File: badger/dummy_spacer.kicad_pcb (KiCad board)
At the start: 2 copper layers, 200 x 200 mm, 12 parts

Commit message: badger upgrades
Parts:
- removed H12: MountingHole, MountingHole:MountingHole_6mm
- moved H11 31.7 mm to (-93.0, 0.00)
- moved H1 2.83 mm to (-93.0, -93.0)
- moved H10 2.83 mm to (-93.0, 93.0)
- moved H4 2.83 mm to (93.0, -93.0)
- moved H7 2.83 mm to (93.0, 93.0)
- moved H2 2.11 mm to (-31.0, -93.0)
- moved H3 2.11 mm to (31.0, -93.0)
- moved H5 2.11 mm to (93.0, -31.0)
- moved H6 2.11 mm to (93.0, 31.0)
- moved H8 2.11 mm to (31.0, 93.0)
- moved H9 2.11 mm to (-31.0, 93.0)
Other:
- outline, holes or cut-outs redrawn

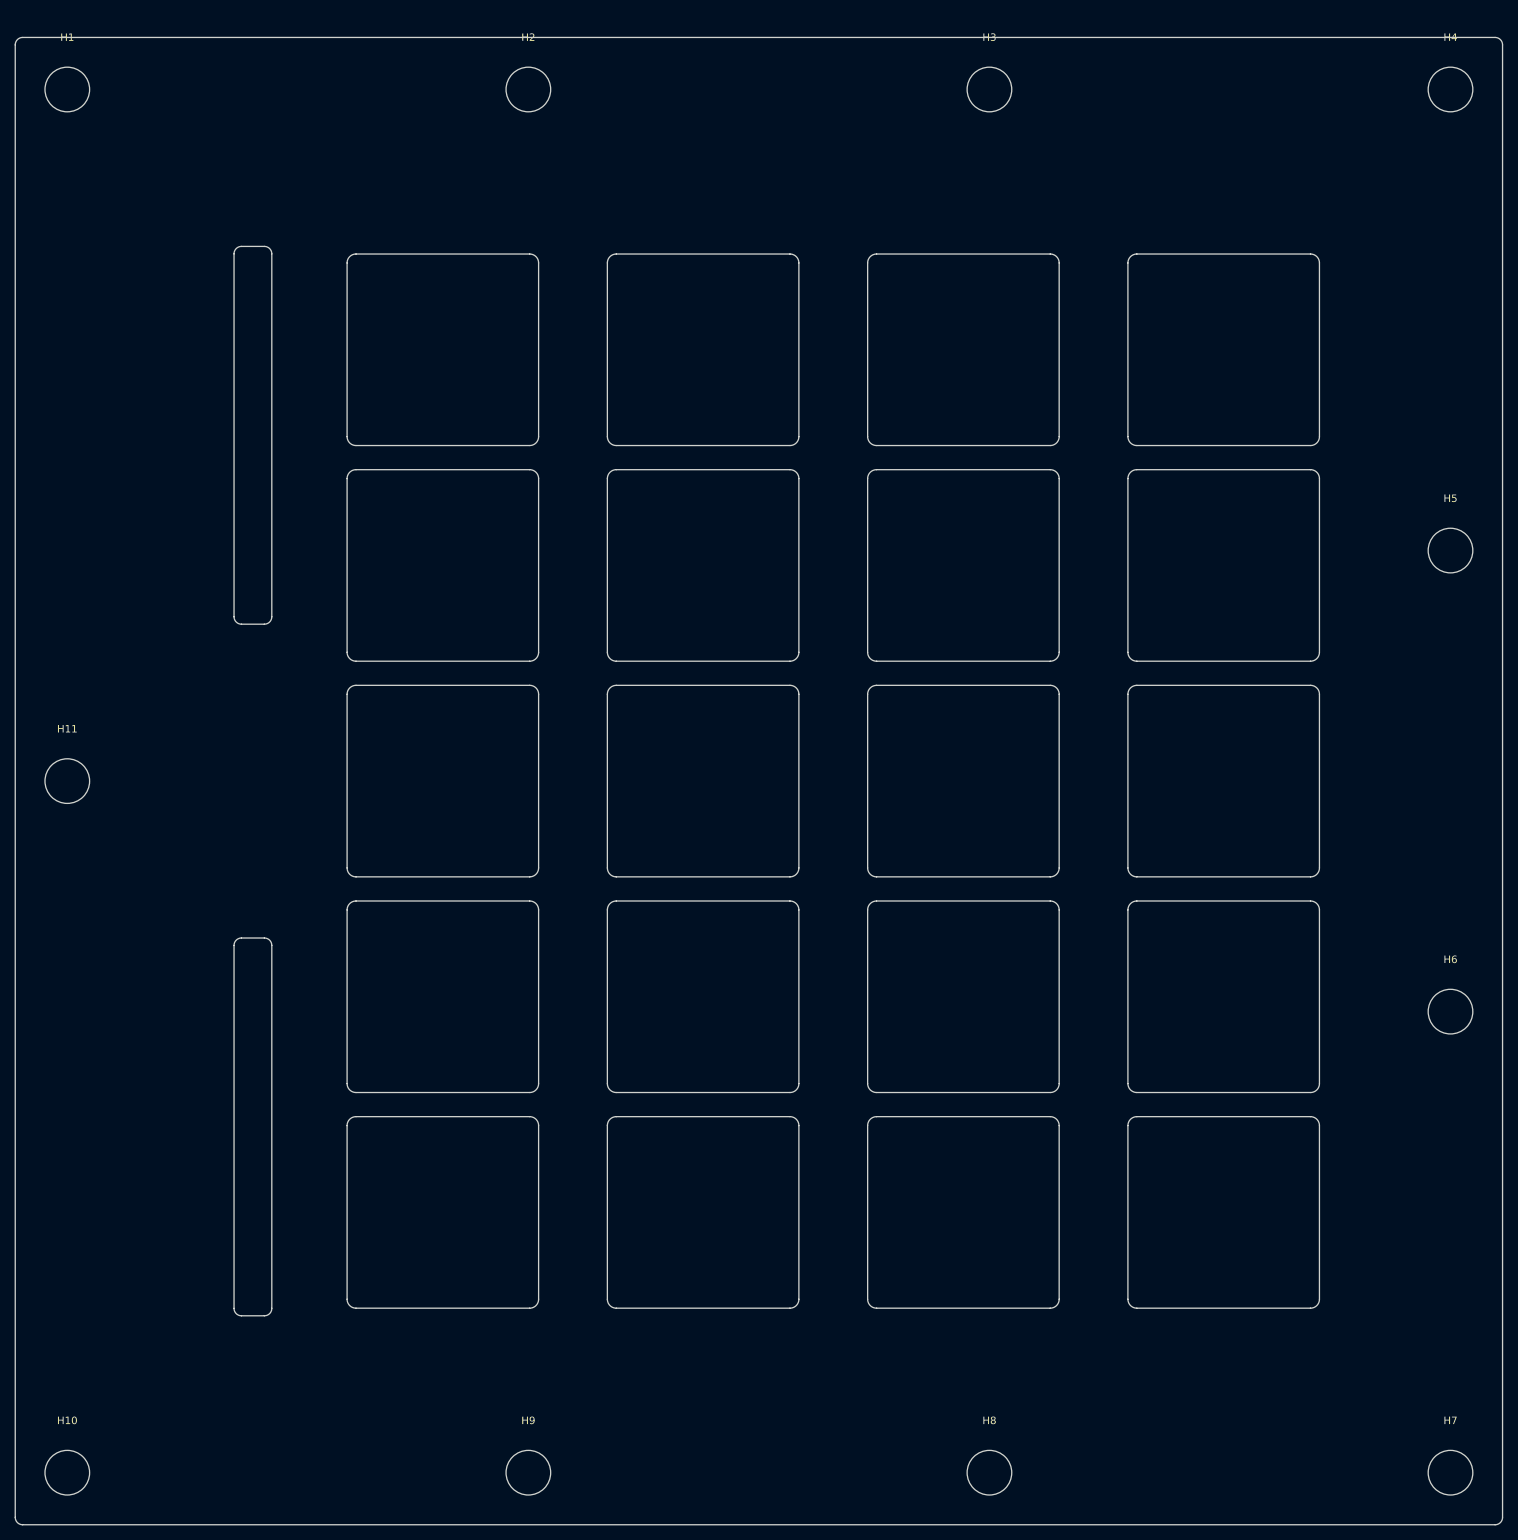
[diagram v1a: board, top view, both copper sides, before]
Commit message: crossbar redesign to get linear trace highway
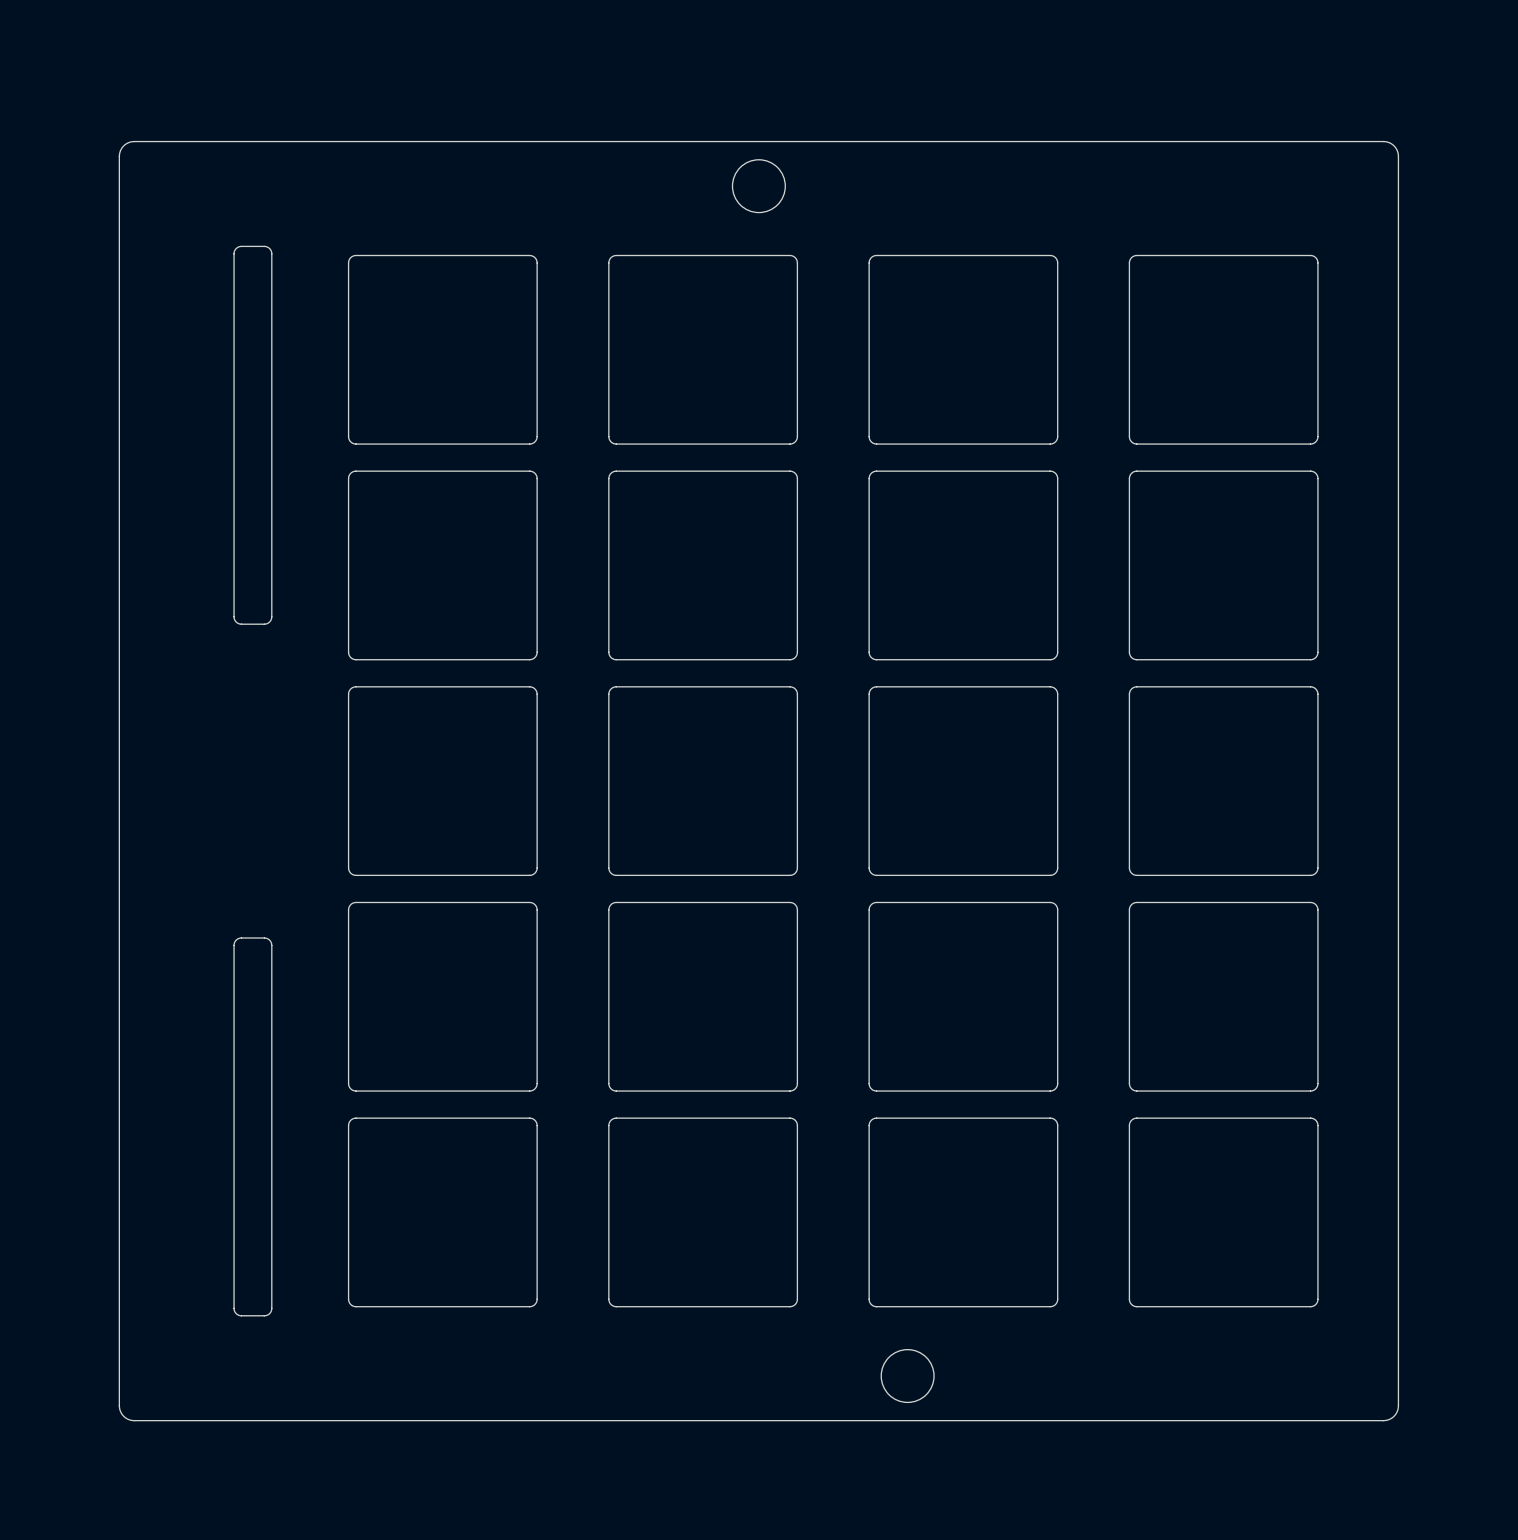
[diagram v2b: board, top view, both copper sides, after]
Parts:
- removed H1, H10, H11, H2, H3, H4, H5, H6, H7, H8, H9: MountingHole, MountingHole:MountingHole_6mm
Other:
- board size 200 x 200 mm -> 172 x 172 mm

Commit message: fab update
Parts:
- added REF**: MountingHole_7.1mm, MINE:MountingHole_7.1mm, F.Cu at (20.0, 80.0)
- added REF**: MountingHole_7.1mm, MINE:MountingHole_7.1mm, F.Cu at (0.00, -80.0)
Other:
- outline, holes or cut-outs redrawn
- board text added: "B.Cu"
- board text added: "F.Cu"
- board text added: "c652367"

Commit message: update silk
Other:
- board text added: "757897f"
- board text removed: "c652367"
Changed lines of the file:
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@@
     (effects (font (size 1.5 1.5) (thickness 0.3)) (justify mirror))
   )
-  (gr_text "c652367" (at -84 -65 -90) (layer "B.SilkS")
+  (gr_text "757897f" (at -84 -65 -90) (layer "B.SilkS")
     (effects (font (size 1 1) (thickness 0.15)) (justify mirror))
   )
-  (gr_text "c652367" (at -84 -65 270) (layer "F.SilkS")
+  (gr_text "757897f" (at -84 -65 270) (layer "F.SilkS")
     (effects (font (size 1 1) (thickness 0.15)))
   )
